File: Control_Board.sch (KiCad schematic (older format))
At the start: 20 parts, among them P1 Batt_Mon, P10 CONN_01X07, P11 Batt, P4 Stearing, P5 D8, P6 V_Sel, P7 A5, P8 Batt_Current, P9 FTDI, U1 LM358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

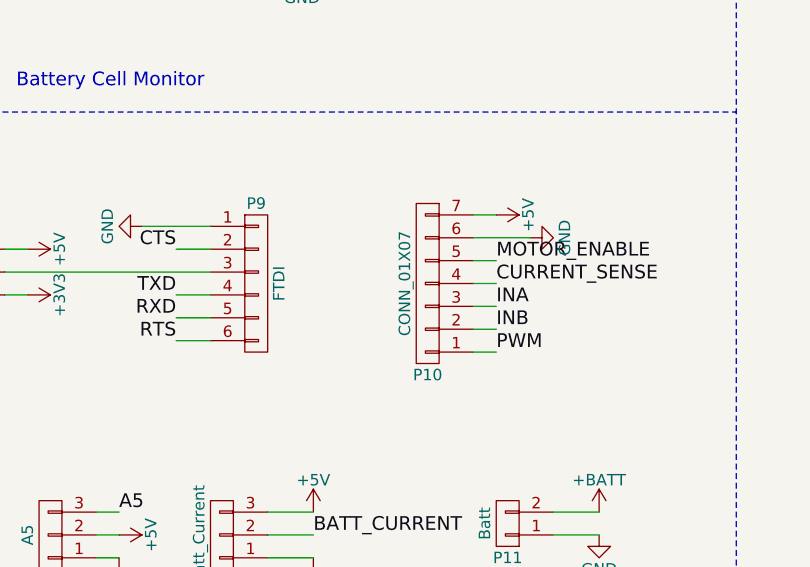
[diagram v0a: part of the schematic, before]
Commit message: Initial layout of the control board to get positioning for making up on some prototyping board.
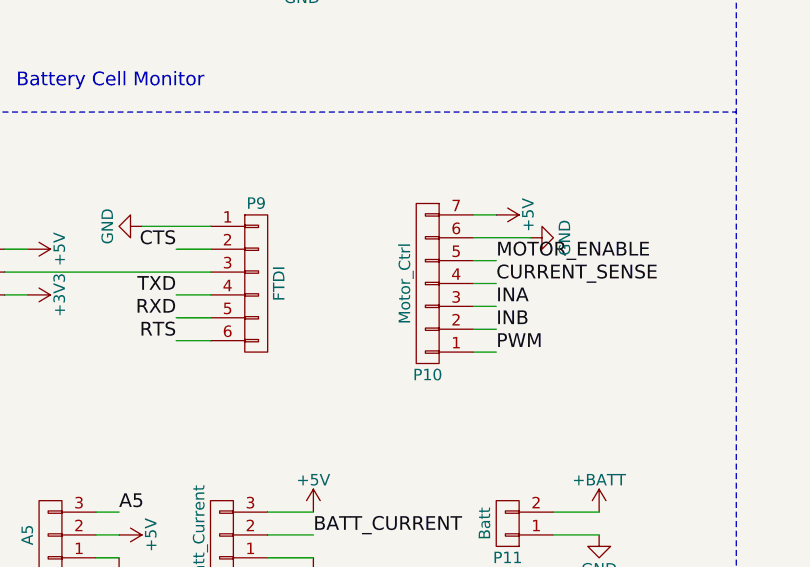
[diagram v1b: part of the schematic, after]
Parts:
- P10: value CONN_01X07 -> Motor_Ctrl; footprint (none) -> Pin_Headers:Pin_Header_Straight_1x07
- P11: footprint (none) -> Pin_Headers:Pin_Header_Straight_1x02
- P8: footprint (none) -> Pin_Headers:Pin_Header_Straight_1x03
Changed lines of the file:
@@
 A2
 $Comp
-L GND #PWR15
+L GND #PWR09
 U 1 1 56BC7C3D
 P 2000 1150
-F 0 "#PWR15" H 2000 900 50  0001 C CNN
+F 0 "#PWR09" H 2000 900 50  0001 C CNN
 F 1 "GND" H 2000 1000 50  0000 C CNN
 F 2 "" H 2000 1150 60  0000 C CNN
@@
 $EndComp
 $Comp
-L GND #PWR29
+L GND #PWR010
 U 1 1 56BC7C43
 P 4200 1150
-F 0 "#PWR29" H 4200 900 50  0001 C CNN
+F 0 "#PWR010" H 4200 900 50  0001 C CNN
 F 1 "GND" H 4200 1000 50  0000 C CNN
 F 2 "" H 4200 1150 60  0000 C CNN
@@
 $EndComp
 $Comp
-L +5V #PWR30
+L +5V #PWR011
 U 1 1 56BC7C49
 P 4200 1950
-F 0 "#PWR30" H 4200 1800 50  0001 C CNN
+F 0 "#PWR011" H 4200 1800 50  0001 C CNN
 F 1 "+5V" H 4200 2090 50  0000 C CNN
 F 2 "" H 4200 1950 60  0000 C CNN
@@
 $EndComp
 $Comp
-L +5V #PWR16
+L +5V #PWR012
 U 1 1 56BC7C4F
 P 2000 1950
-F 0 "#PWR16" H 2000 1800 50  0001 C CNN
+F 0 "#PWR012" H 2000 1800 50  0001 C CNN
 F 1 "+5V" H 2000 2090 50  0000 C CNN
 F 2 "" H 2000 1950 60  0000 C CNN
@@
 $EndComp
 $Comp
-L +5V #PWR34
+L +5V #PWR013
 U 1 1 56BC7C55
 P 9100 2200
-F 0 "#PWR34" H 9100 2050 50  0001 C CNN
+F 0 "#PWR013" H 9100 2050 50  0001 C CNN
 F 1 "+5V" H 9100 2340 50  0000 C CNN
 F 2 "" H 9100 2200 60  0000 C CNN
@@
 $EndComp
 $Comp
-L GND #PWR33
+L GND #PWR014
 U 1 1 56BC7C5B
 P 9100 2000
-F 0 "#PWR33" H 9100 1750 50  0001 C CNN
+F 0 "#PWR014" H 9100 1750 50  0001 C CNN
 F 1 "GND" H 9100 1850 50  0000 C CNN
 F 2 "" H 9100 2000 60  0000 C CNN
@@
 $EndComp
 $Comp
-L GND #PWR28
+L GND #PWR015
 U 1 1 56BC7C99
 P 3700 2050
-F 0 "#PWR28" H 3700 1800 50  0001 C CNN
+F 0 "#PWR015" H 3700 1800 50  0001 C CNN
 F 1 "GND" H 3700 1900 50  0000 C CNN
 F 2 "" H 3700 2050 60  0000 C CNN
@@
 $EndComp
 $Comp
-L GND #PWR13
+L GND #PWR016
 U 1 1 56BC7C9F
 P 1500 2050
-F 0 "#PWR13" H 1500 1800 50  0001 C CNN
+F 0 "#PWR016" H 1500 1800 50  0001 C CNN
 F 1 "GND" H 1500 1900 50  0000 C CNN
 F 2 "" H 1500 2050 60  0000 C CNN
@@
 A0
 $Comp
-L +BATT #PWR35
+L +BATT #PWR017
 U 1 1 56BC7CAC
 P 9250 1900
-F 0 "#PWR35" H 9250 1750 50  0001 C CNN
+F 0 "#PWR017" H 9250 1750 50  0001 C CNN
 F 1 "+BATT" H 9250 2040 50  0000 C CNN
 F 2 "" H 9250 1900 60  0000 C CNN
@@
 	5600 500  5600 5500
 $Comp
-L +3V3 #PWR36
+L +3V3 #PWR018
 U 1 1 56BC7CE2
 P 9250 2300
-F 0 "#PWR36" H 9250 2150 50  0001 C CNN
+F 0 "#PWR018" H 9250 2150 50  0001 C CNN
 F 1 "+3V3" H 9250 2440 50  0000 C CNN
 F 2 "" H 9250 2300 50  0000 C CNN
@@
 Cell3
 $Comp
-L GND #PWR9
+L GND #PWR019
 U 1 1 56BC8371
 P 1350 3550
-F 0 "#PWR9" H 1350 3300 50  0001 C CNN
+F 0 "#PWR019" H 1350 3300 50  0001 C CNN
 F 1 "GND" H 1350 3400 50  0000 C CNN
 F 2 "" H 1350 3550 60  0000 C CNN
@@
 STEAR
 $Comp
-L +5V #PWR10
+L +5V #PWR020
 U 1 1 56BC8383
 P 1400 4550
-F 0 "#PWR10" H 1400 4400 50  0001 C CNN
+F 0 "#PWR020" H 1400 4400 50  0001 C CNN
 F 1 "+5V" H 1400 4690 50  0000 C CNN
 F 2 "" H 1400 4550 50  0000 C CNN
@@
 $EndComp
 $Comp
-L GND #PWR12
+L GND #PWR021
 U 1 1 56BC8389
 P 1450 4650
-F 0 "#PWR12" H 1450 4400 50  0001 C CNN
+F 0 "#PWR021" H 1450 4400 50  0001 C CNN
 F 1 "GND" H 1450 4500 50  0000 C CNN
 F 2 "" H 1450 4650 50  0000 C CNN
@@
 $EndComp
 $Comp
-L +3V3 #PWR32
+L +3V3 #PWR022
 U 1 1 56BC85AC
 P 7700 3700
-F 0 "#PWR32" H 7700 3550 50  0001 C CNN
+F 0 "#PWR022" H 7700 3550 50  0001 C CNN
 F 1 "+3V3" H 7700 3840 50  0000 C CNN
 F 2 "" H 7700 3700 50  0000 C CNN
@@
 $EndComp
 $Comp
-L GND #PWR31
+L GND #PWR023
 U 1 1 56BC85B2
 P 7550 3550
-F 0 "#PWR31" H 7550 3300 50  0001 C CNN
+F 0 "#PWR023" H 7550 3300 50  0001 C CNN
 F 1 "GND" H 7550 3400 50  0000 C CNN
 F 2 "" H 7550 3550 50  0000 C CNN
@@
 $EndComp
 $Comp
-L +5V #PWR21
+L +5V #PWR024
 U 1 1 56BC85D4
 P 2900 4550
-F 0 "#PWR21" H 2900 4400 50  0001 C CNN
+F 0 "#PWR024" H 2900 4400 50  0001 C CNN
 F 1 "+5V" H 2900 4690 50  0000 C CNN
 F 2 "" H 2900 4550 50  0000 C CNN
@@
 $EndComp
 $Comp
-L +5V #PWR17
+L +5V #PWR025
 U 1 1 56BC85DA
 P 2150 4550
-F 0 "#PWR17" H 2150 4400 50  0001 C CNN
+F 0 "#PWR025" H 2150 4400 50  0001 C CNN
 F 1 "+5V" H 2150 4690 50  0000 C CNN
 F 2 "" H 2150 4550 50  0000 C CNN
@@
 $EndComp
 $Comp
-L GND #PWR18
+L GND #PWR026
 U 1 1 56BC85E0
 P 2150 4650
-F 0 "#PWR18" H 2150 4400 50  0001 C CNN
+F 0 "#PWR026" H 2150 4400 50  0001 C CNN
 F 1 "GND" H 2150 4500 50  0000 C CNN
 F 2 "" H 2150 4650 50  0000 C CNN
@@
 $EndComp
 $Comp
-L GND #PWR22
+L GND #PWR027
 U 1 1 56BC85E6
 P 2900 4650
-F 0 "#PWR22" H 2900 4400 50  0001 C CNN
+F 0 "#PWR027" H 2900 4400 50  0001 C CNN
 F 1 "GND" H 2900 4500 50  0000 C CNN
 F 2 "" H 2900 4650 50  0000 C CNN
@@
 $EndComp
 $Comp
-L GND #PWR23
+L GND #PWR028
 U 1 1 56BC8772
 P 3000 3200
-F 0 "#PWR23" H 3000 2950 50  0001 C CNN
+F 0 "#PWR028" H 3000 2950 50  0001 C CNN
 F 1 "GND" H 3000 3050 50  0000 C CNN
 F 2 "" H 3000 3200 50  0000 C CNN
@@
 	3150 3300 3300 3300
 $Comp
-L +5V #PWR19
+L +5V #PWR029
 U 1 1 56BC877B
 P 2500 3300
-F 0 "#PWR19" H 2500 3150 50  0001 C CNN
+F 0 "#PWR029" H 2500 3150 50  0001 C CNN
 F 1 "+5V" H 2500 3440 50  0000 C CNN
 F 2 "" H 2500 3300 50  0000 C CNN
@@
 $EndComp
 $Comp
-L +3V3 #PWR20
+L +3V3 #PWR030
 U 1 1 56BC878F
 P 2500 3500
-F 0 "#PWR20" H 2500 3350 50  0001 C CNN
+F 0 "#PWR030" H 2500 3350 50  0001 C CNN
 F 1 "+3V3" H 2500 3640 50  0000 C CNN
 F 2 "" H 2500 3500 50  0000 C CNN
@@
 F 0 "P8" H 3350 4750 50  0000 C CNN
 F 1 "Batt_Current" V 3450 4550 50  0000 C CNN
-F 2 "" H 3350 4550 50  0000 C CNN
+F 2 "Pin_Headers:Pin_Header_Straight_1x03" H 3350 4550 50  0001 C CNN
 F 3 "" H 3350 4550 50  0000 C CNN
 	1    3350 4550
@@
 $EndComp
 $Comp
-L +5V #PWR24
+L +5V #PWR031
 U 1 1 56BC94B1
 P 3000 6200
-F 0 "#PWR24" H 3000 6050 50  0001 C CNN
+F 0 "#PWR031" H 3000 6050 50  0001 C CNN
 F 1 "+5V" H 3000 6340 50  0000 C CNN
 F 2 "" H 3000 6200 50  0000 C CNN
@@
 $EndComp
 $Comp
-L GND #PWR25
+L GND #PWR032
 U 1 1 56BC94EB
 P 3000 6400
-F 0 "#PWR25" H 3000 6150 50  0001 C CNN
+F 0 "#PWR032" H 3000 6150 50  0001 C CNN
 F 1 "GND" H 3000 6250 50  0000 C CNN
 F 2 "" H 3000 6400 50  0000 C CNN
@@
 	2800 6300 3000 6300
 $Comp
-L GND #PWR14
+L GND #PWR033
 U 1 1 56BC9C6D
 P 1550 6300
-F 0 "#PWR14" H 1550 6050 50  0001 C CNN
+F 0 "#PWR033" H 1550 6050 50  0001 C CNN
 F 1 "GND" H 1550 6150 50  0000 C CNN
 F 2 "" H 1550 6300 60  0000 C CNN
@@
 $EndComp
 $Comp
-L +5V #PWR11
+L +5V #PWR034
 U 1 1 56BC9C73
 P 1400 6200
-F 0 "#PWR11" H 1400 6050 50  0001 C CNN
+F 0 "#PWR034" H 1400 6050 50  0001 C CNN
 F 1 "+5V" H 1400 6340 50  0000 C CNN
 F 2 "" H 1400 6200 60  0000 C CNN
@@
 P 4250 3450
 F 0 "P10" H 4250 3850 50  0000 C CNN
-F 1 "CONN_01X07" V 4350 3450 50  0000 C CNN
-F 2 "" H 4250 3450 50  0000 C CNN
+F 1 "Motor_Ctrl" V 4350 3450 50  0000 C CNN
+F 2 "Pin_Headers:Pin_Header_Straight_1x07" H 4250 3450 50  0001 C CNN
 F 3 "" H 4250 3450 50  0000 C CNN
 	1    4250 3450
@@
 F 0 "P11" H 4600 4650 50  0000 C CNN
 F 1 "Batt" V 4700 4500 50  0000 C CNN
-F 2 "" H 4600 4500 50  0000 C CNN
+F 2 "Pin_Headers:Pin_Header_Straight_1x02" H 4600 4500 50  0001 C CNN
 F 3 "" H 4600 4500 50  0000 C CNN
 	1    4600 4500
@@
 GND
 $Comp
-L +BATT #PWR26
+L +BATT #PWR035
 U 1 1 56BCC39C
 P 3000 6900
-F 0 "#PWR26" H 3000 6750 50  0001 C CNN
+F 0 "#PWR035" H 3000 6750 50  0001 C CNN
 F 1 "+BATT" H 3000 7040 50  0000 C CNN
 F 2 "" H 3000 6900 50  0000 C CNN
@@
 $EndComp
 $Comp
-L GND #PWR27
+L GND #PWR036
 U 1 1 56BCC3DA
 P 3000 7000
-F 0 "#PWR27" H 3000 6750 50  0001 C CNN
+F 0 "#PWR036" H 3000 6750 50  0001 C CNN
 F 1 "GND" H 3000 6850 50  0000 C CNN
 F 2 "" H 3000 7000 50  0000 C CNN
@@
 	3000 6900 2800 6900
 $Comp
-L GND #PWR?
+L GND #PWR037
 U 1 1 56BCFDFD
 P 4700 3250
-F 0 "#PWR?" H 4700 3000 50  0001 C CNN
+F 0 "#PWR037" H 4700 3000 50  0001 C CNN
 F 1 "GND" H 4700 3100 50  0000 C CNN
 F 2 "" H 4700 3250 60  0000 C CNN
@@
 $EndComp
 $Comp
-L +5V #PWR?
+L +5V #PWR038
 U 1 1 56BCFE03
 P 4550 3150
-F 0 "#PWR?" H 4550 3000 50  0001 C CNN
+F 0 "#PWR038" H 4550 3000 50  0001 C CNN
 F 1 "+5V" H 4550 3290 50  0000 C CNN
 F 2 "" H 4550 3150 60  0000 C CNN
@@
 	4450 3750 4550 3750
 $Comp
-L +BATT #PWR?
+L +BATT #PWR039
 U 1 1 56BCFE4D
 P 5000 4450
-F 0 "#PWR?" H 5000 4300 50  0001 C CNN
+F 0 "#PWR039" H 5000 4300 50  0001 C CNN
 F 1 "+BATT" H 5000 4590 50  0000 C CNN
 F 2 "" H 5000 4450 50  0000 C CNN
@@
 $EndComp
 $Comp
-L GND #PWR?
+L GND #PWR040
 U 1 1 56BCFE53
 P 5000 4550
-F 0 "#PWR?" H 5000 4300 50  0001 C CNN
+F 0 "#PWR040" H 5000 4300 50  0001 C CNN
 F 1 "GND" H 5000 4400 50  0000 C CNN
 F 2 "" H 5000 4550 50  0000 C CNN
@@
 	5000 4450 4800 4450
 $Comp
-L +5V #PWR?
+L +5V #PWR041
 U 1 1 56BCFE95
 P 3750 4450
-F 0 "#PWR?" H 3750 4300 50  0001 C CNN
+F 0 "#PWR041" H 3750 4300 50  0001 C CNN
 F 1 "+5V" H 3750 4590 50  0000 C CNN
 F 2 "" H 3750 4450 50  0000 C CNN
@@
 $EndComp
 $Comp
-L GND #PWR?
+L GND #PWR042
 U 1 1 56BCFE9B
 P 3750 4650
-F 0 "#PWR?" H 3750 4400 50  0001 C CNN
+F 0 "#PWR042" H 3750 4400 50  0001 C CNN
 F 1 "GND" H 3750 4500 50  0000 C CNN
 F 2 "" H 3750 4650 50  0000 C CNN

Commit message: Modified to use a simple voltage divider for battery voltage measurement, the op amp version would not fit on the prototype board and not really needed. Also added headers to allow the FTDI TX/RX to be swapped.
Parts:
- removed R1, R3, R5, R6, R7, R8: 10K, Resistors_ThroughHole:Resistor_Horizontal_RM10mm, symbol R
- removed U1: LM358, Housings_DIP:DIP-8_W7.62mm, symbol LM358-RESCUE-BACONdriver
- added P12: Cross, Pin_Headers:Pin_Header_Straight_2x02, symbol CONN_02X02
- added P13: A5, Pin_Headers:Pin_Header_Straight_1x03, symbol CONN_01X03
- P1: symbol CONN_01X04 -> CONN_01X03
- P7: value A5 -> A4
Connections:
- net A2 is gone; now on net CS_VAL: U4.8 (A2)
- net +5V: now also P13.2 (P2)
- net A0: no longer R2.2
- net A1: now also R2.1, R4.2
- net A5: now also P13.3 (P3); no longer P7.3 (P3)
- net CS_VAL: no longer U4.6 (A3)
- net Cell2: now also R2.2
- net GND: now also P13.1 (P1)
- net MOTOR_CURRENT: now also U4.6 (A3); no longer U4.4 (A4)
- net RXD: now also P12.1 (P1); no longer P9.5 (P5)
- net TXD: now also P12.4 (P4); no longer P9.4 (P4)
- removed net Cell3: P1.4 (P4)
- new net: P12.3 (P3), P9.4 (P4)
- new net: P12.2 (P2), P9.5 (P5)
- new net A4: P7.3 (P3), U4.4 (A4)
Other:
- moved on the sheet: P10, P11, P4, P5, P6, P7, P8, P9, R2, R4
